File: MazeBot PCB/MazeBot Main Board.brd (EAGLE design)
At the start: 76.2 x 45.4 mm, 43 parts, among them IC1 7805TV, IC2 L298, Q1 16MHz

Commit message: Minor fixes
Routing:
- net GND: track 14.9 -> 15.1 mm, vias 70 -> 72

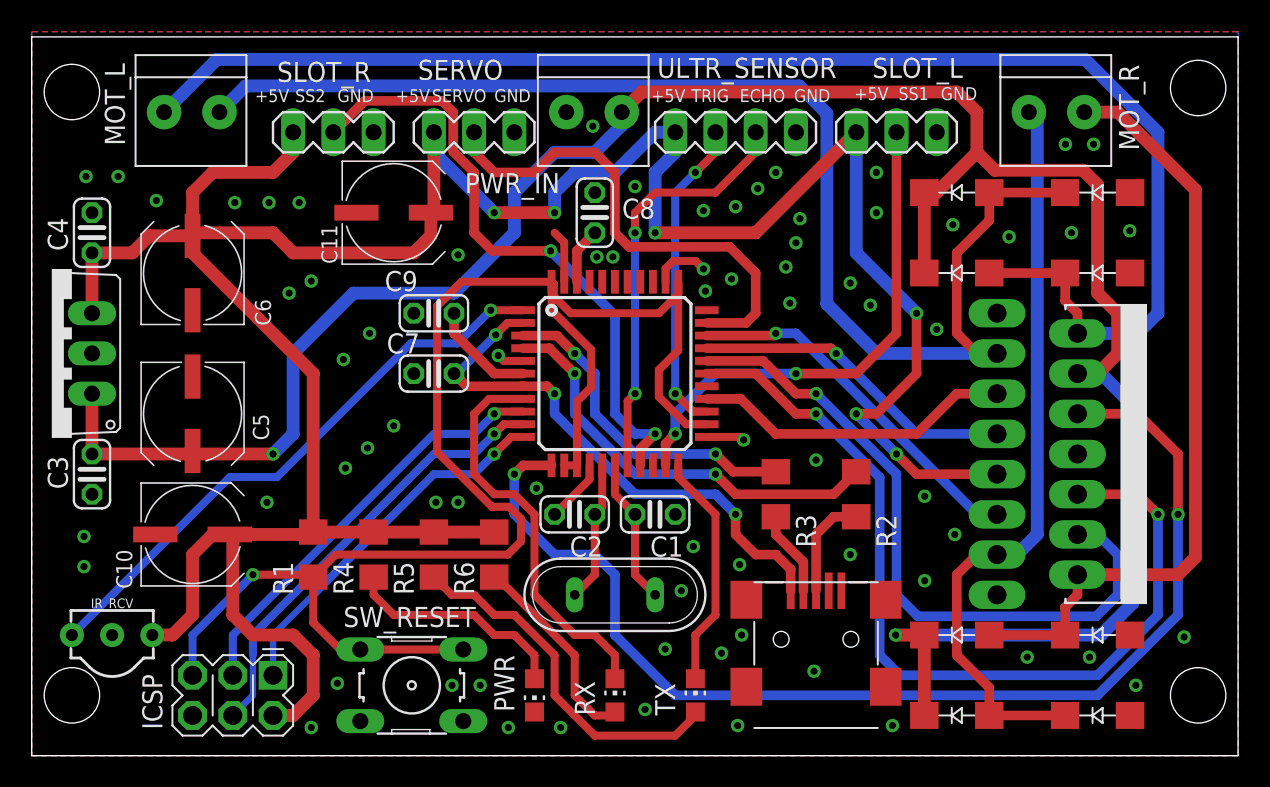
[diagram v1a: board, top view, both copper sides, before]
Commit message: Add HWB grounding
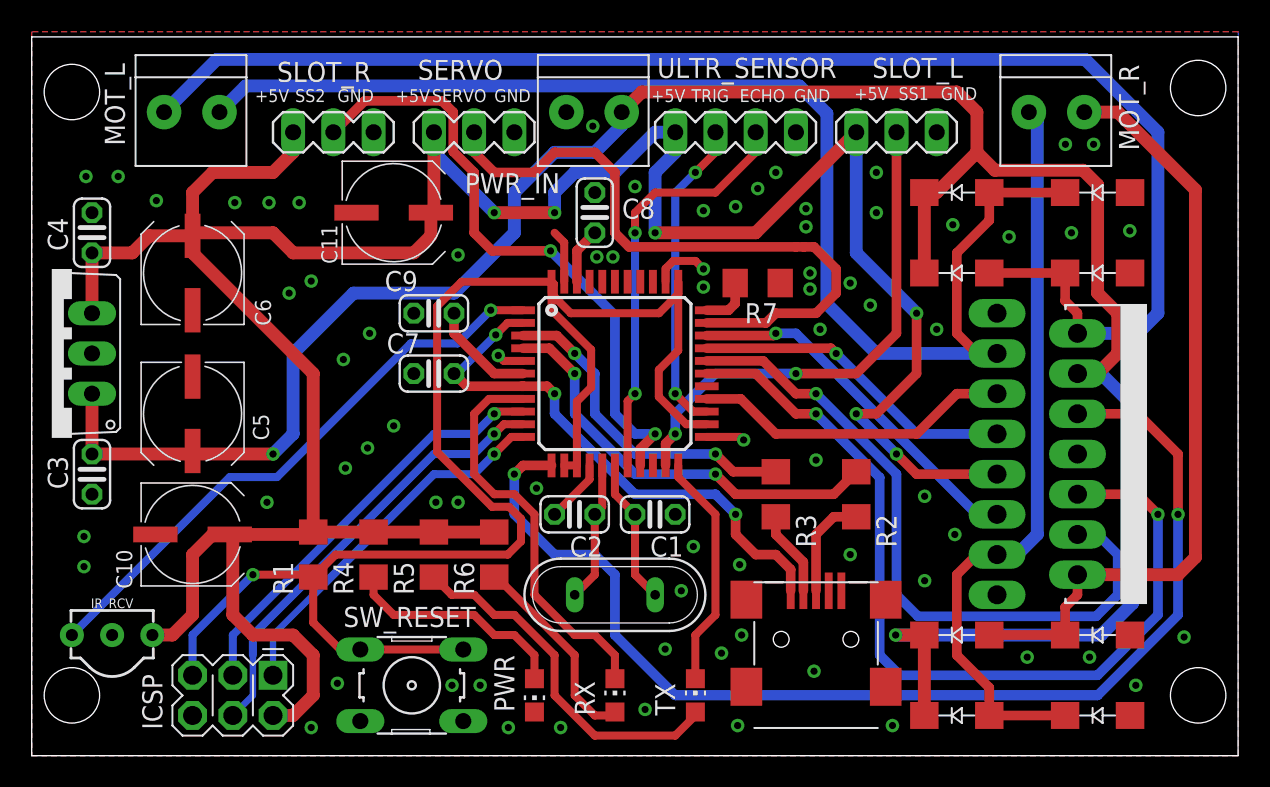
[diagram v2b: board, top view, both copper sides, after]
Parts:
- added R7: 10k, eagle-ltspice:R1206
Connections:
- new net N$8: R7.2, U$1.33
- net GND: now also R7.1
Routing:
- net EN_L: track 73.7 -> 100.3 mm
- net SERVO: track 31.4 -> 40.9 mm
- net N$8: track 0.00 -> 3.26 mm
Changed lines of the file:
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@@
 <attribute name="VALUE" x="46.22" y="0" size="1.27" layer="27"/>
+</element>
+<element name="R7" library="eagle-ltspice" library_urn="urn:adsk.eagle:library:217" package="R1206" package3d_urn="urn:adsk.eagle:package:13301/1" value="10k" x="45.847" y="29.845" smashed="yes" rot="R180">
+<attribute name="NAME" x="47.117" y="28.575" size="1.27" layer="25" rot="R180"/>
+<attribute name="SPICEMODEL" value="NONE" x="45.847" y="29.845" size="1.778" layer="27" rot="R180" display="off"/>
+<attribute name="SPICEPREFIX" value="R" x="45.847" y="29.845" size="1.778" layer="27" rot="R180" display="off"/>
+<attribute name="VALUE" x="47.117" y="32.385" size="1.27" layer="27" rot="R180"/>
 </element>
 </elements>
@@
 <via x="36.703" y="31.496" extent="1-16" drill="0.45"/>
 <via x="42.418" y="30.734" extent="1-16" drill="0.45"/>
-<via x="44.196" y="30.099" extent="1-16" drill="0.45"/>
-<via x="42.545" y="29.337" extent="1-16" drill="0.45"/>
-<via x="48.26" y="32.385" extent="1-16" drill="0.45"/>
-<via x="48.514" y="33.909" extent="1-16" drill="0.45"/>
-<via x="47.625" y="30.861" extent="1-16" drill="0.45"/>
-<via x="47.879" y="28.575" extent="1-16" drill="0.45"/>
+<via x="48.895" y="34.544" extent="1-16" drill="0.45"/>
+<via x="48.895" y="33.401" extent="1-16" drill="0.45"/>
+<via x="49.784" y="26.924" extent="1-16" drill="0.45"/>
 <via x="42.418" y="34.417" extent="1-16" drill="0.45"/>
 <via x="44.45" y="34.671" extent="1-16" drill="0.45"/>
@@
 <via x="25.527" y="16.002" extent="1-16" drill="0.45"/>
 <via x="26.924" y="16.002" extent="1-16" drill="0.45"/>
+<contactref element="R7" pad="1"/>
+<via x="49.149" y="29.464" extent="1-16" drill="0.45"/>
+<via x="49.149" y="30.48" extent="1-16" drill="0.45"/>
+<via x="42.418" y="29.591" extent="1-16" drill="0.45"/>
 </signal>
 <signal name="EN_L">
@@
 <wire x1="30.48" y1="17.78" x2="31.03" y2="18.33" width="0.6096" layer="1"/>
 <wire x1="31.03" y1="18.33" x2="32.83" y2="18.33" width="0.6096" layer="1"/>
+<wire x1="67.31" y1="3.81" x2="40.64" y2="3.81" width="0.6096" layer="16"/>
 </signal>
 <signal name="EN_R">
@@
 <contactref element="U$1" pad="32"/>
 <contactref element="SERVO" pad="2"/>
-<wire x1="42.63" y1="27.33" x2="45.11" y2="27.33" width="0.6096" layer="1"/>
-<wire x1="45.11" y1="27.33" x2="45.72" y2="27.94" width="0.6096" layer="1"/>
-<wire x1="45.72" y1="27.94" x2="45.72" y2="30.48" width="0.6096" layer="1"/>
-<wire x1="45.72" y1="30.48" x2="44.069" y2="32.131" width="0.6096" layer="1"/>
-<wire x1="44.069" y1="32.131" x2="37.719" y2="32.131" width="0.6096" layer="1"/>
 <wire x1="37.719" y1="32.131" x2="36.83" y2="33.02" width="0.6096" layer="1"/>
 <wire x1="36.83" y1="36.83" x2="35.56" y2="38.1" width="0.6096" layer="1"/>
@@
 <wire x1="27.94" y1="38.1" x2="27.94" y2="39.37" width="0.6096" layer="1"/>
 <wire x1="36.83" y1="33.02" x2="36.83" y2="36.83" width="0.6096" layer="1"/>
+<wire x1="42.63" y1="27.33" x2="46.38" y2="27.33" width="0.6096" layer="1"/>
+<wire x1="46.38" y1="27.33" x2="46.99" y2="27.94" width="0.6096" layer="1"/>
+<wire x1="48.768" y1="32.131" x2="48.26" y2="32.131" width="0.6096" layer="1"/>
+<wire x1="48.26" y1="32.131" x2="37.719" y2="32.131" width="0.6096" layer="1"/>
+<wire x1="48.768" y1="32.131" x2="49.403" y2="32.131" width="0.6096" layer="1"/>
+<wire x1="50.8" y1="30.734" x2="50.8" y2="29.21" width="0.6096" layer="1"/>
+<wire x1="50.8" y1="29.21" x2="49.53" y2="27.94" width="0.6096" layer="1"/>
+<wire x1="49.53" y1="27.94" x2="46.99" y2="27.94" width="0.6096" layer="1"/>
+<wire x1="49.403" y1="32.131" x2="50.8" y2="30.734" width="0.6096" layer="1"/>
 </signal>
 <signal name="ULTR_TRIG">
@@
 <via x="51.689" y="12.7" extent="1-16" drill="0.45"/>
 </signal>
+<signal name="N$8">
+<contactref element="U$1" pad="33"/>
+<contactref element="R7" pad="2"/>
+<wire x1="44.425" y1="29.845" x2="44.425" y2="28.55" width="0.6096" layer="1"/>
+<wire x1="44.005" y1="28.13" x2="42.63" y2="28.13" width="0.6096" layer="1"/>
+<wire x1="44.425" y1="28.55" x2="44.005" y2="28.13" width="0.6096" layer="1"/>
+</signal>
 </signals>

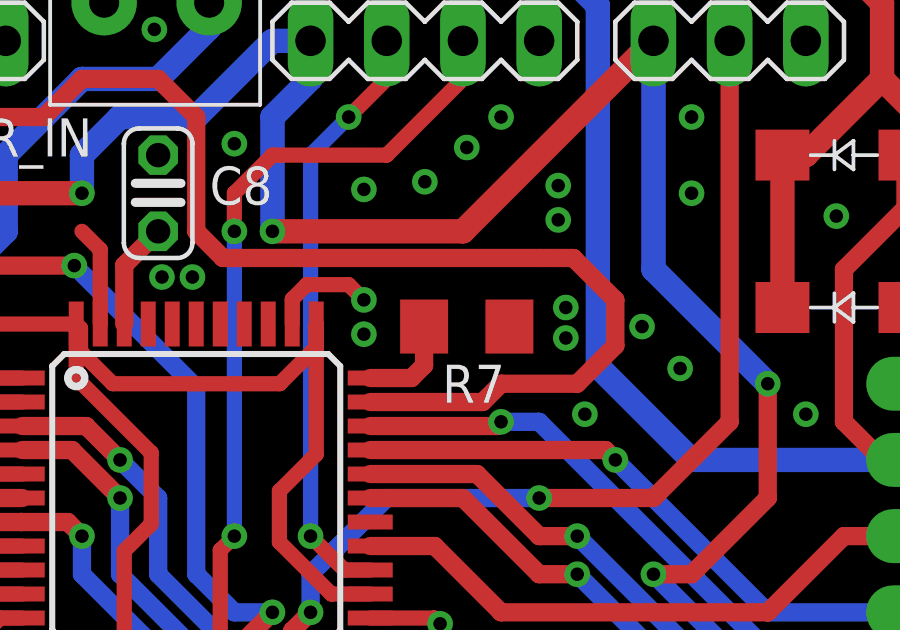
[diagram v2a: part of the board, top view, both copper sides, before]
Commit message: Add jumper to HWB
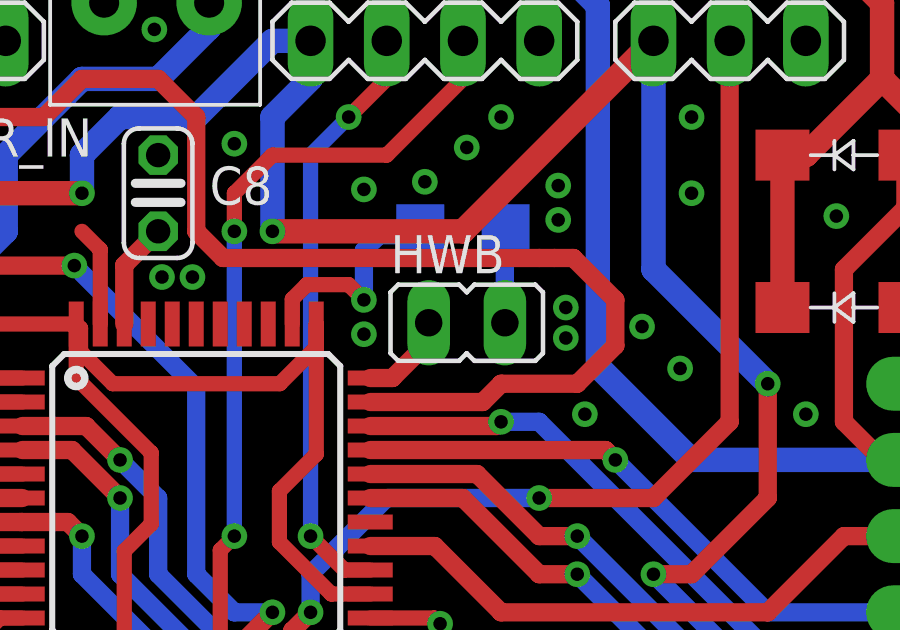
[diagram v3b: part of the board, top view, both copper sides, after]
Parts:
- added HWB: (no value), jumper:JP1
- moved R7 3.18 mm to (45.7, 33.0), flipped to the bottom
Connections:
- new net N$9: HWB.2, R7.2
- net N$8: now also HWB.1; no longer R7.2
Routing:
- net GND: track 15.1 -> 18.9 mm
- net N$9: track 0.00 -> 3.06 mm
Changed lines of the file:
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@@
 <drawing>
 <settings>
-<setting alwaysvectorfont="yes"/>
+<setting alwaysvectorfont="no"/>
 <setting verticaltext="up"/>
 </settings>
@@
 <attribute name="VALUE" x="46.22" y="0" size="1.27" layer="27"/>
 </element>
-<element name="R7" library="eagle-ltspice" library_urn="urn:adsk.eagle:library:217" package="R1206" package3d_urn="urn:adsk.eagle:package:13301/1" value="10k" x="45.847" y="29.845" smashed="yes" rot="R180">
-<attribute name="NAME" x="47.117" y="28.575" size="1.27" layer="25" rot="R180"/>
-<attribute name="SPICEMODEL" value="NONE" x="45.847" y="29.845" size="1.778" layer="27" rot="R180" display="off"/>
-<attribute name="SPICEPREFIX" value="R" x="45.847" y="29.845" size="1.778" layer="27" rot="R180" display="off"/>
-<attribute name="VALUE" x="47.117" y="32.385" size="1.27" layer="27" rot="R180"/>
+<element name="R7" library="eagle-ltspice" library_urn="urn:adsk.eagle:library:217" package="R1206" package3d_urn="urn:adsk.eagle:package:13301/1" value="10k" x="45.72" y="33.02" smashed="yes" rot="MR180">
+<attribute name="NAME" x="44.45" y="31.75" size="1.27" layer="26" rot="MR180"/>
+<attribute name="SPICEMODEL" value="NONE" x="45.72" y="33.02" size="1.778" layer="28" rot="MR180" display="off"/>
+<attribute name="SPICEPREFIX" value="R" x="45.72" y="33.02" size="1.778" layer="28" rot="MR180" display="off"/>
+<attribute name="VALUE" x="44.45" y="35.56" size="1.27" layer="28" rot="MR180"/>
+</element>
+<element name="HWB" library="jumper" library_urn="urn:adsk.eagle:library:252" package="JP1" package3d_urn="urn:adsk.eagle:package:15455/1" value="" x="45.847" y="29.972" smashed="yes" rot="R270">
+<attribute name="NAME" x="43.307" y="31.623" size="1.27" layer="25" ratio="10"/>
+<attribute name="VALUE" x="43.307" y="27.051" size="1.27" layer="27" ratio="10"/>
 </element>
 </elements>
@@
 <via x="49.149" y="30.48" extent="1-16" drill="0.45"/>
 <via x="42.418" y="29.591" extent="1-16" drill="0.45"/>
+<wire x1="42.418" y1="30.734" x2="42.418" y2="32.385" width="0.6096" layer="16"/>
+<wire x1="42.418" y1="32.385" x2="42.926" y2="32.893" width="0.6096" layer="16"/>
+<wire x1="42.926" y1="32.893" x2="44.171" y2="32.893" width="0.6096" layer="16"/>
+<wire x1="44.171" y1="32.893" x2="44.298" y2="33.02" width="0.6096" layer="16"/>
 </signal>
 <signal name="EN_L">
@@
 <signal name="N$8">
 <contactref element="U$1" pad="33"/>
+<contactref element="HWB" pad="1"/>
+<wire x1="44.577" y1="29.972" x2="44.577" y2="29.337" width="0.6096" layer="1"/>
+<wire x1="44.577" y1="29.337" x2="43.37" y2="28.13" width="0.6096" layer="1"/>
+<wire x1="43.37" y1="28.13" x2="42.63" y2="28.13" width="0.6096" layer="1"/>
+</signal>
+<signal name="N$9">
+<contactref element="HWB" pad="2"/>
 <contactref element="R7" pad="2"/>
-<wire x1="44.425" y1="29.845" x2="44.425" y2="28.55" width="0.6096" layer="1"/>
-<wire x1="44.005" y1="28.13" x2="42.63" y2="28.13" width="0.6096" layer="1"/>
-<wire x1="44.425" y1="28.55" x2="44.005" y2="28.13" width="0.6096" layer="1"/>
+<wire x1="47.117" y1="29.972" x2="47.117" y2="32.995" width="0.6096" layer="16"/>
+<wire x1="47.117" y1="32.995" x2="47.142" y2="33.02" width="0.6096" layer="16"/>
 </signal>
 </signals>

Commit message: Fix XTAL caps
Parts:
- C1, C2: value 100nF -> 22pF
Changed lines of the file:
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@@
 </autorouter>
 <elements>
-<element name="C1" library="rcl" library_urn="urn:adsk.eagle:library:334" package="C025-024X044" package3d_urn="urn:adsk.eagle:package:23630/1" value="100nF" x="39.37" y="15.24" smashed="yes" rot="R180">
+<element name="C1" library="rcl" library_urn="urn:adsk.eagle:library:334" package="C025-024X044" package3d_urn="urn:adsk.eagle:package:23630/1" value="22pF" x="39.37" y="15.24" smashed="yes" rot="R180">
 <attribute name="NAME" x="41.148" y="13.843" size="1.27" layer="25" ratio="10" rot="R180"/>
 <attribute name="SPICEPREFIX" value="C" x="15.24" y="68.58" size="1.778" layer="27" rot="R180" display="off"/>
@@
 <attribute name="VALUE" x="19.304" y="34.29" size="1.016" layer="27" rot="R90"/>
 </element>
-<element name="C2" library="rcl" library_urn="urn:adsk.eagle:library:334" package="C025-024X044" package3d_urn="urn:adsk.eagle:package:23630/1" value="100nF" x="34.29" y="15.24" smashed="yes" rot="R180">
+<element name="C2" library="rcl" library_urn="urn:adsk.eagle:library:334" package="C025-024X044" package3d_urn="urn:adsk.eagle:package:23630/1" value="22pF" x="34.29" y="15.24" smashed="yes" rot="R180">
 <attribute name="NAME" x="36.068" y="13.843" size="1.27" layer="25" ratio="10" rot="R180"/>
 <attribute name="SPICEPREFIX" value="C" x="3.81" y="68.58" size="1.778" layer="27" rot="R180" display="off"/>

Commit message: PCB print day upload
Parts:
- added L1: 600Ω/500mA, SparkFun-Coils:0805
- C3, C4: value 100nF -> 0.1uF
- C5: value 47uF -> 0.33uF; device rcl:UD-6,3X5,8_NICHICON -> rcl:UD-4X5,8_NICHICON
- C6: value 47uF -> 0.1uF; device rcl:UD-6,3X5,8_NICHICON -> rcl:C025-024X044
- moved C3 66.2 mm to (68.2, 33.0), turned to 0 degrees
- moved C4 55.8 mm to (57.1, 16.6), turned to 270 degrees
- moved MOT_L 1.14 mm to (11.3, 40.6)
- moved IR_RCV 0.64 mm to (5.08, 8.26)
- moved C6 0.38 mm to (10.2, 30.9), turned to 270 degrees
- moved C5 0.13 mm to (10.2, 21.7)
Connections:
- new net N$10: L1.1, USB.VBUS
- net +5V: now also C6.1, U$1.14, U$1.24, U$1.34, U$1.44; no longer C6.+
- net GND: now also C6.2; no longer C6.-
- net RESET: no longer U$1.14, U$1.24, U$1.34, U$1.44
- net UVCC: now also L1.2; no longer USB.VBUS
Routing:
- net RESET: track 100.3 -> 41.0 mm, vias 1 -> 2
- net +5V: track 185.3 -> 230.5 mm
- net UVCC: track 35.0 -> 30.8 mm
- net V+: track 149.5 -> 146.2 mm
- net N$10: track 0.00 -> 3.07 mm
- net MOT2_L: track 81.4 -> 80.3 mm
- net MOT1_L: track 92.0 -> 90.9 mm
- net EN_R: track 23.1 -> 24.2 mm
- net GND: track 18.9 -> 19.6 mm, vias 72 -> 69

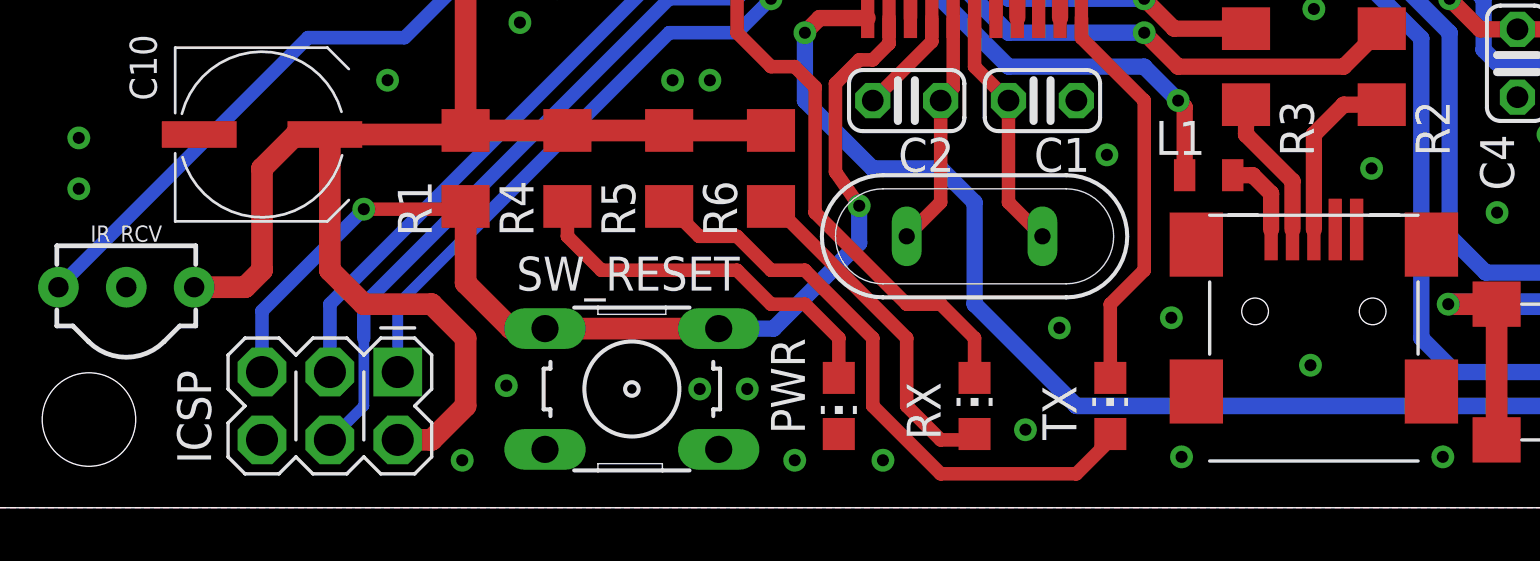
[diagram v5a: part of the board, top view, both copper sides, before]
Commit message: Final schamtic cleanup for documentation
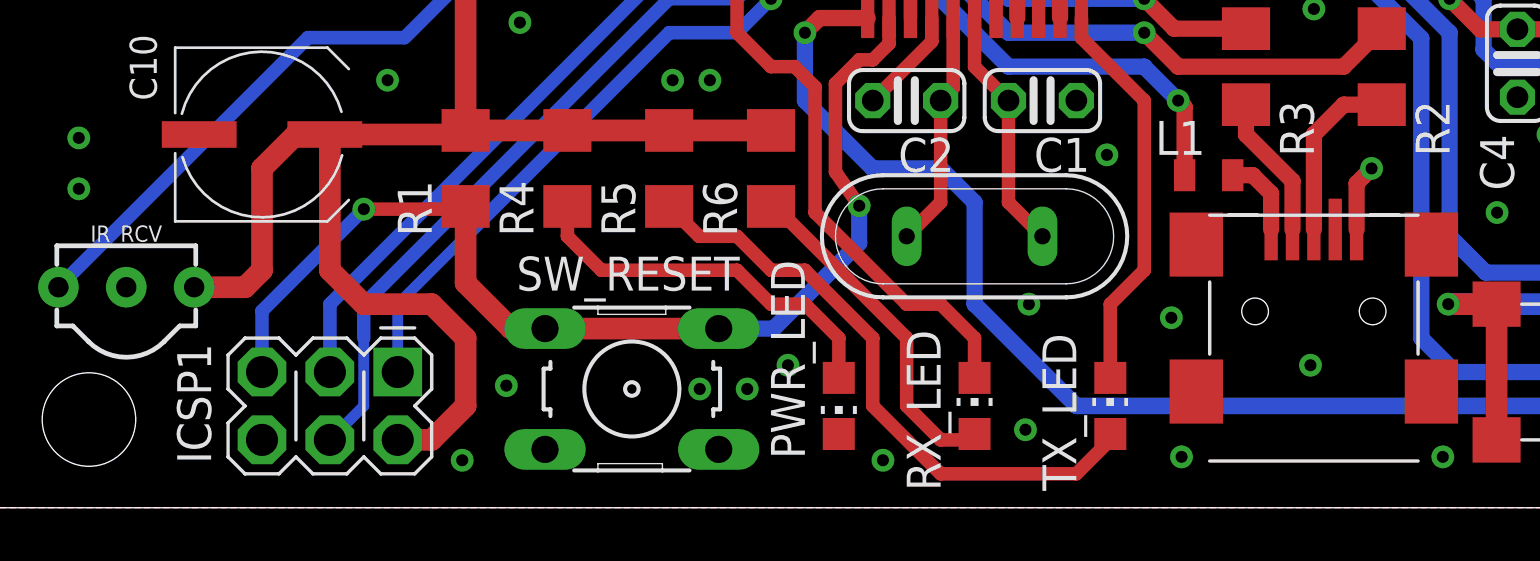
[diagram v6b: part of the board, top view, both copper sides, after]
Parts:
- renumbered IC1 to U1, IC2 to U2, ICSP to ICSP1, PWR to PWR_LED, RX to RX_LED, TX to TX_LED, U$1 to U3
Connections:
- net TX_LED renamed TX
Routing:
- net GND: track 19.6 -> 22.2 mm
